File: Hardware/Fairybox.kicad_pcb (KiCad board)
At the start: 2 copper layers, 91.4 x 55.9 mm, 70 parts, among them J1 REED, Q1 locked, Q10 locked, Q2 locked, Q3 locked, Q4 locked, Q5 locked, Q6 locked, Q7 locked, Q8 locked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

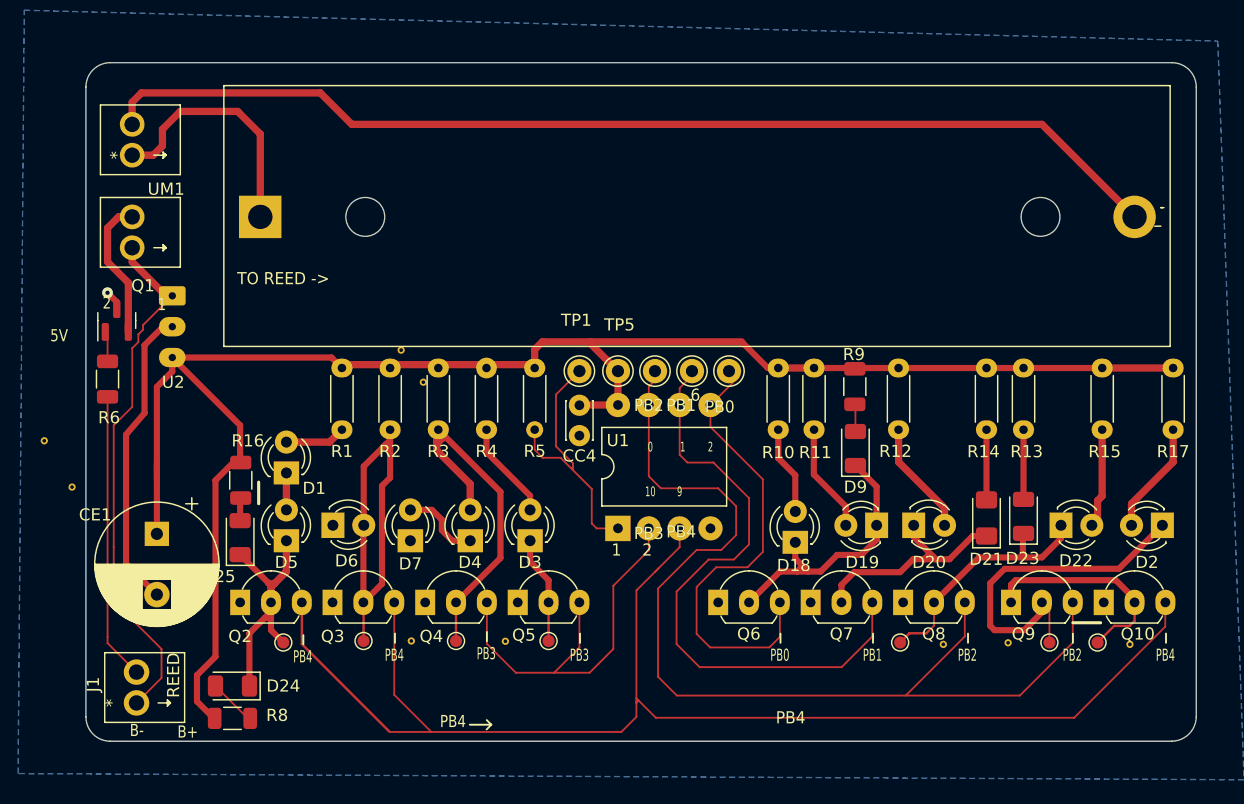
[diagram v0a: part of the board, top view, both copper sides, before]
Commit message: Power Delivery  EEschema   - Added two 1x2P 2.5mm pitch pin header symbols with associated footprints to replace the custom liion charge breakout board symbol/footprints   - Moved liion charge board and n-channel mosfet south on the board to make room for:   - Shifted 18650 battery sled from the right of the board to the center, allowing room for some SMD leds around the board periphery.  PCBnew   - New lion charge board pin headers
MCU
 EEschema
  - Added 220R series resistors (R7, R18, R19) to each MCU pin used for SPI in circuit programming. Protects the programmer GPIO pins from voltages greater than 22mA
 PCBnew
  - 220R series resistors added to SPI lines at the bottom of the board. Shifted tracks around a little to get them to fit. The resistors will be under the exclusion zone, but they're small so it's okay.

Lighting
 PCBnew
  - Rotated LED D4 so the leads can be bent without running into it's neighbour
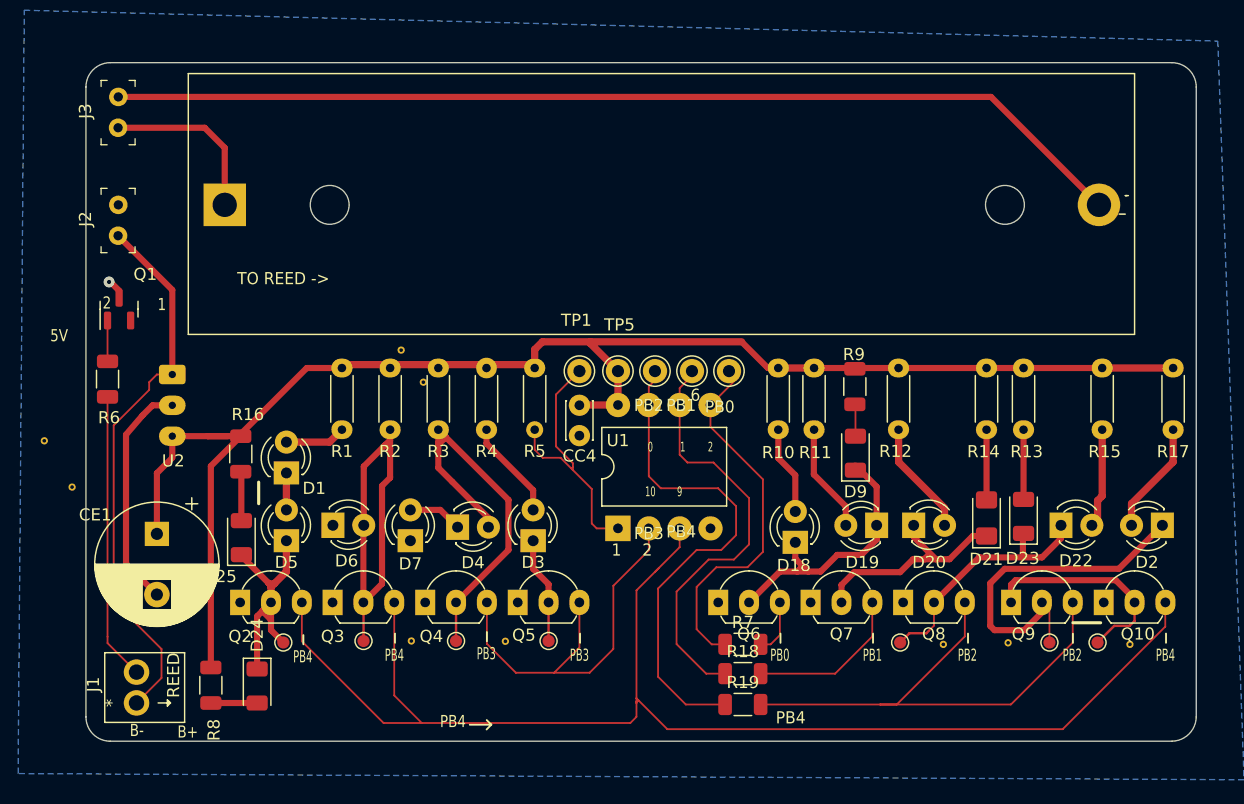
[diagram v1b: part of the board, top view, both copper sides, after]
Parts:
- removed UM1: HW-107, UltraLibrary:HW-107 2.54mm terminals
- added J2: 640456-2, digikey-footprints:PinHeader_1x2_P2.54mm, F.Cu at (53.4, 65.0)
- added J3: 640456-2, digikey-footprints:PinHeader_1x2_P2.54mm, F.Cu at (53.4, 56.2)
- added R18: 220R, Resistor_SMD:R_1206_3216Metric, F.Cu at (104.9, 101.1)
- added R19: 220R, Resistor_SMD:R_1206_3216Metric, F.Cu at (104.9, 103.7)
- added R7: 220R, Resistor_SMD:R_1206_3216Metric, F.Cu at (104.9, 98.7)
- R8: value ??R -> 470R
- moved U2 6.48 mm to (57.9, 76.5)
- moved R8 3.26 mm to (61.1, 102.1), turned to -90 degrees
- moved BAT1 3.09 mm to (62.2, 61.7)
- moved R16 2.17 mm to (63.6, 83.0)
- moved D24 2.03 mm to (64.9, 102.1), turned to -90 degrees
- moved D4 1.53 mm to (81.4, 89.1), turned to 0 degrees
- moved Q1 0.96 mm to (53.5, 71.1)
- moved D9 0.38 mm to (114.2, 83.0)
- moved D3 0.25 mm to (87.6, 90.2)
- moved D25 0.10 mm to (63.6, 89.9)
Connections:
- net Net-(D4-Pad1) renamed /D7_AN
- TP2 pad 1: /MCU GPIO2 SCK -> /7
- TP3 pad 1: /MCU GPIO1 MISO -> /6
- TP4 pad 1: /MCU GPIO0 MOSI -> /5
- U1 pad 5: /MCU GPIO0 MOSI -> /5
- U1 pad 6: /MCU GPIO1 MISO -> /6
- U1 pad 7: /MCU GPIO2 SCK -> /7
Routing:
- net /7: track 0.00 -> 40.7 mm
- net /MCU GPIO2 SCK: track 83.4 -> 42.8 mm
- net /MCU GPIO1 MISO: track 50.9 -> 13.1 mm
- net /6: track 0.00 -> 35.4 mm
- net /MCU GPIO0 MOSI: track 37.6 -> 4.59 mm
- net /5: track 0.00 -> 29.6 mm
- net +5V: track 153.6 -> 135.7 mm
- net /CHARGE BOARD OUT B-: track 11.7 -> 0.00 mm
- net /LI-ION_POS: track 20.4 -> 14.2 mm
- net GND: track 26.0 -> 20.8 mm
- net /LI-ION_NEG: track 88.9 -> 84.4 mm
- net /CHARGE BOARD OUT B+: track 42.8 -> 45.6 mm
- net /Q4_COL: track 29.4 -> 32.1 mm
- net /D25_AN: track 1.81 -> 4.05 mm
- net /D7_AN: track 6.49 -> 4.48 mm
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
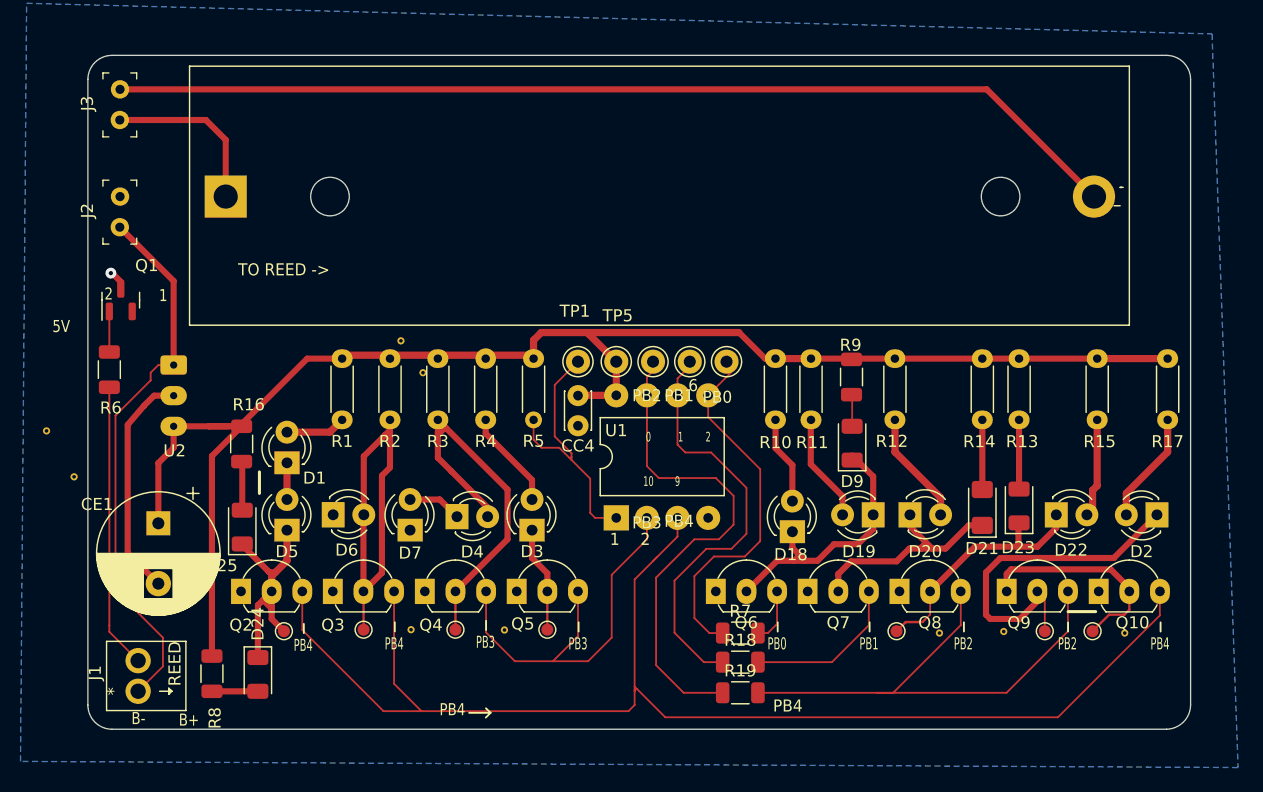
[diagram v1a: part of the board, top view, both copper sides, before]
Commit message: JST connector, Rule Zone Added JST PH connector instead of screw terminals. Corrected keepout zone.
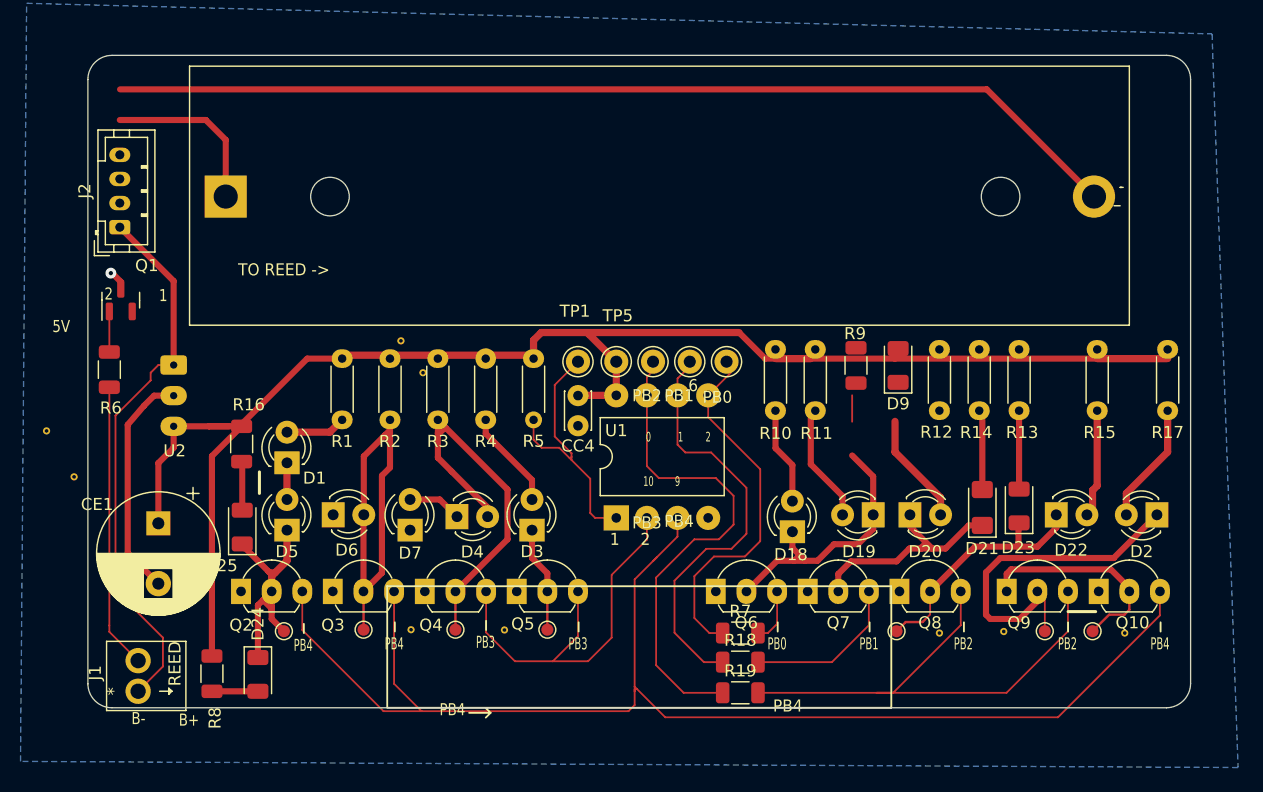
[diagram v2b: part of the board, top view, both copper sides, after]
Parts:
- removed J3: 640456-2, digikey-footprints:PinHeader_1x2_P2.54mm
- J2: value 640456-2 -> JST B4B-PH-K-S; footprint digikey-footprints:PinHeader_1x2_P2.54mm -> Connector_JST:JST_PH_B4B-PH-K_1x04_P2.00mm_Vertical
- moved D9 7.49 mm to (118.0, 76.5)
- moved R12 3.77 mm to (121.4, 75.2)
- moved R9 1.03 mm to (114.5, 76.5)
- moved R11 0.84 mm to (111.1, 75.2)
- moved R14 0.80 mm to (124.7, 75.2)
- moved R10 0.76 mm to (107.8, 75.2)
- moved R13 0.76 mm to (128.0, 75.2)
- moved R15 0.76 mm to (134.5, 75.2)
- moved R17 0.76 mm to (140.3, 75.2)
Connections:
- J2 pad 1: /CHARGE BOARD OUT B+ -> /LI-ION_POS
- J2 pad 2: /CHARGE BOARD OUT B- -> /LI-ION_NEG
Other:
- board size 91.4 x 55.9 mm -> 91.4 x 54.1 mm
